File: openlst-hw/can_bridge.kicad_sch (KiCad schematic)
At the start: 1 part, among them J9 Conn_01x05_Pin

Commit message: propate the changes to RF
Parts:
- J9: Part Number (none) -> generic; now fitted
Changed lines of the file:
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@@
 		(in_bom yes)
 		(on_board yes)
-		(dnp yes)
+		(dnp no)
 		(property "Reference" "J9"
 			(at 200.025 52.705 0)
@@
 			(at 200.66 62.865 0)
 			(effects
+				(font
+					(size 1.27 1.27)
+				)
+				(hide yes)
+			)
+		)
+		(property "Part Number" "generic"
+			(at 200.66 62.865 0)
+			(effects

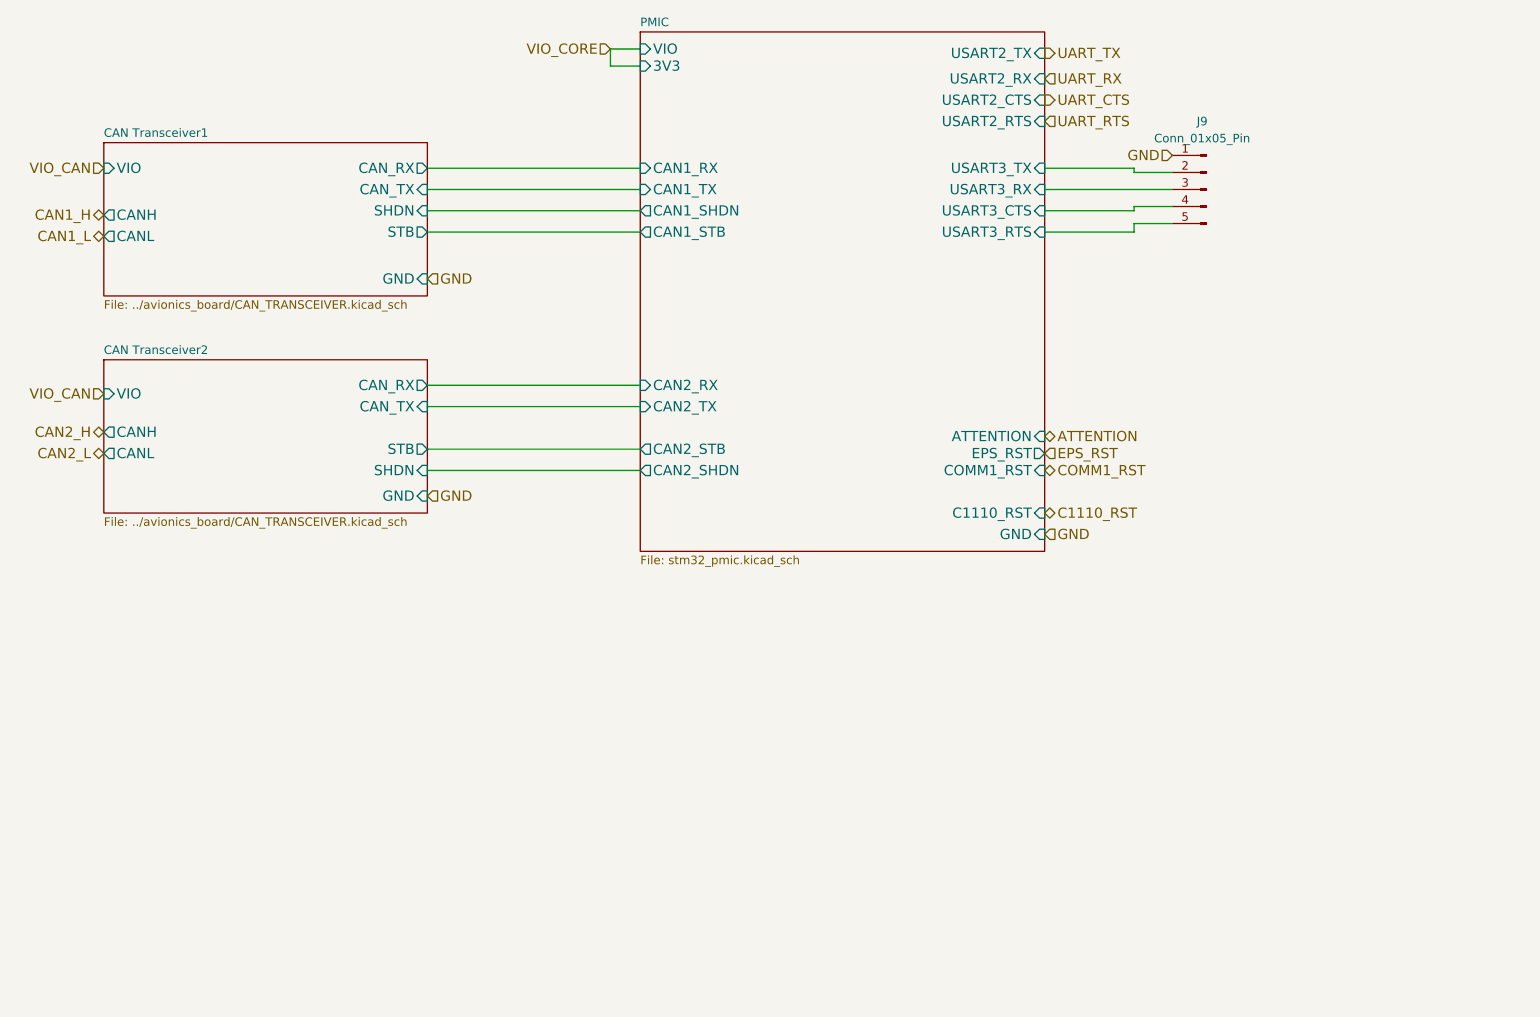
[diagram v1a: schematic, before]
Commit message: local switches and monitors for SCI and RF
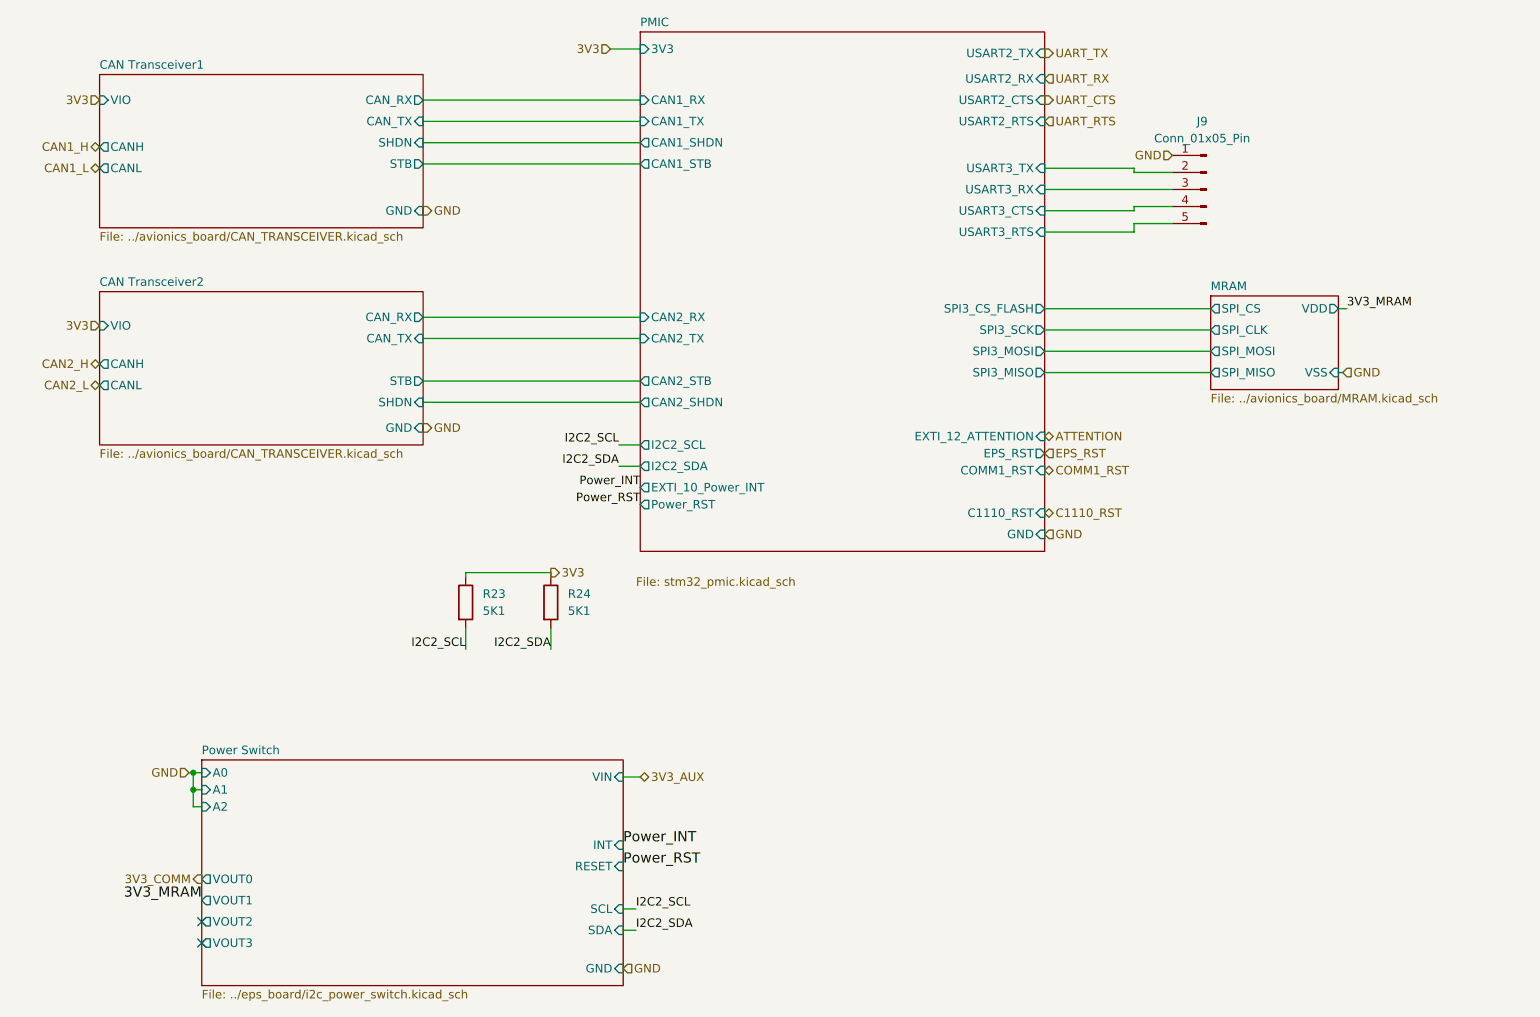
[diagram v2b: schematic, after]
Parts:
- added R23, R24: 5K1, Resistor_SMD:R_0402_1005Metric_Pad0.72x0.64mm_HandSolder, symbol Device:R
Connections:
- new net 3V3: R23.1, R24.1
- new net I2C2_SCL: R23.2
- new net I2C2_SDA: R24.2
- no-connect marks 0 -> 2
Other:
- added sheet MRAM (../avionics_board/MRAM.kicad_sch)
- added sheet Power Switch (../eps_board/i2c_power_switch.kicad_sch)
- sheet PMIC ports: added EXTI_10_Power_INT, EXTI_12_ATTENTION, I2C2_SCL, I2C2_SDA, Power_RST, SPI3_CS_FLASH, SPI3_MISO, SPI3_MOSI, SPI3_SCK; removed ATTENTION, VIO
